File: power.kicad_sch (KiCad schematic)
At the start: 50 parts, among them J8 DeployLipo, J9 UCLipo, Q6 SI4143DY-T1-GE3, Q7 SI4143DY-T1-GE3, U10 NCP1117-3.3_SOT223, U11 XC8111, U12 XC8111, U13 XC8111, U14 LTC4412xS6, U15 MAX77827AEFD+T, U16 SC4215, U17 LTC4412xS6, U18 XC8111, U9 XC8111

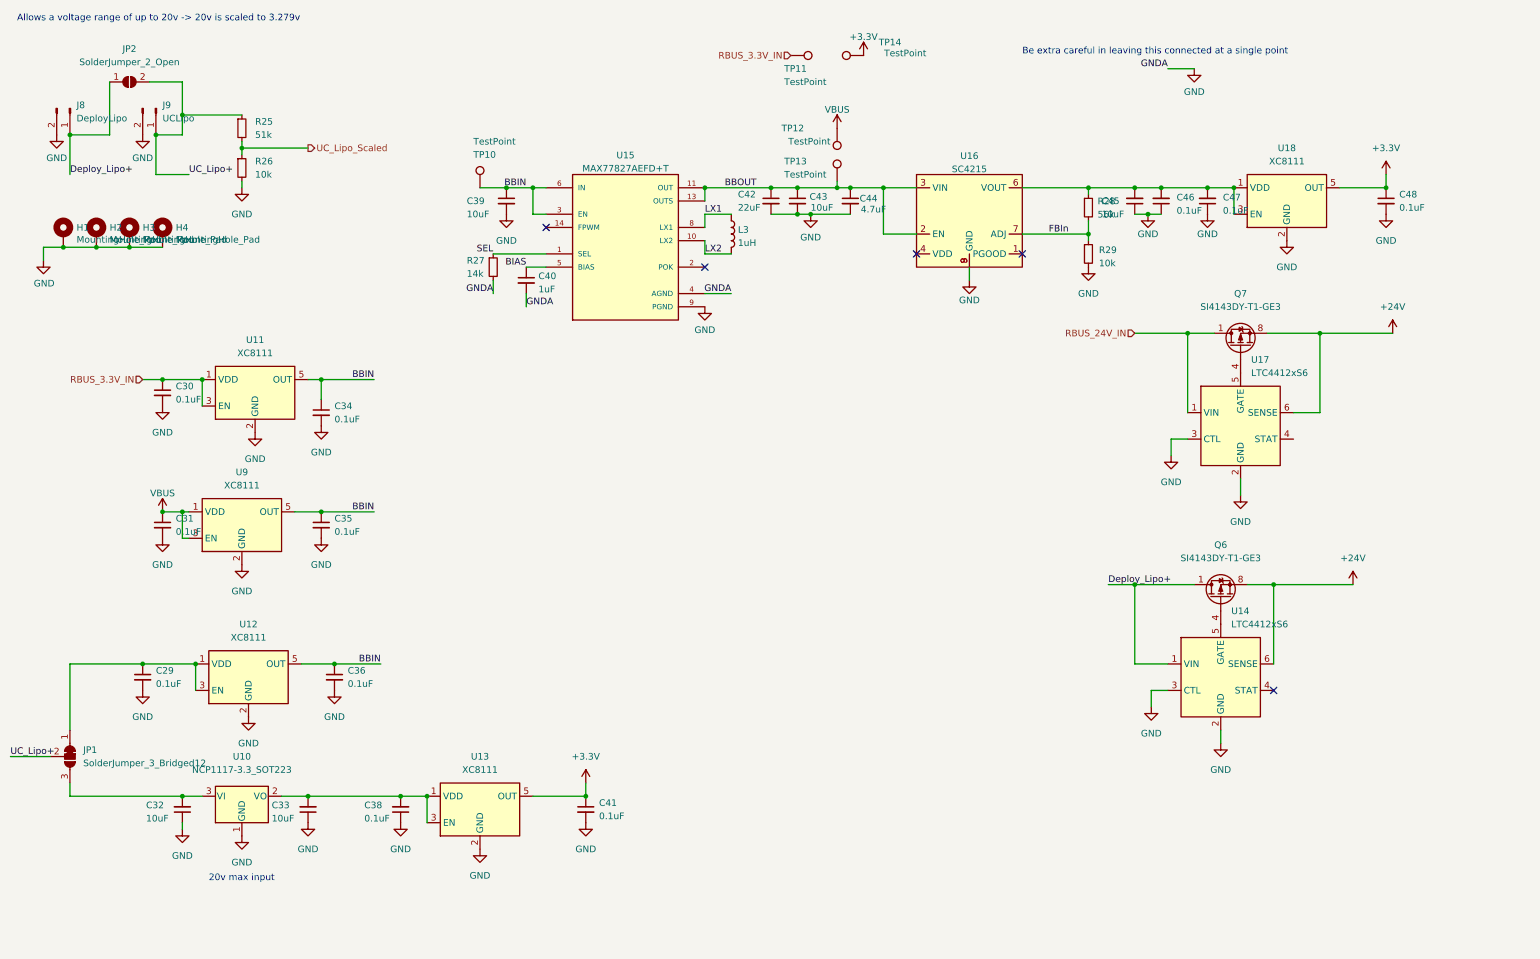
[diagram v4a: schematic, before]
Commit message: changed bb and power side
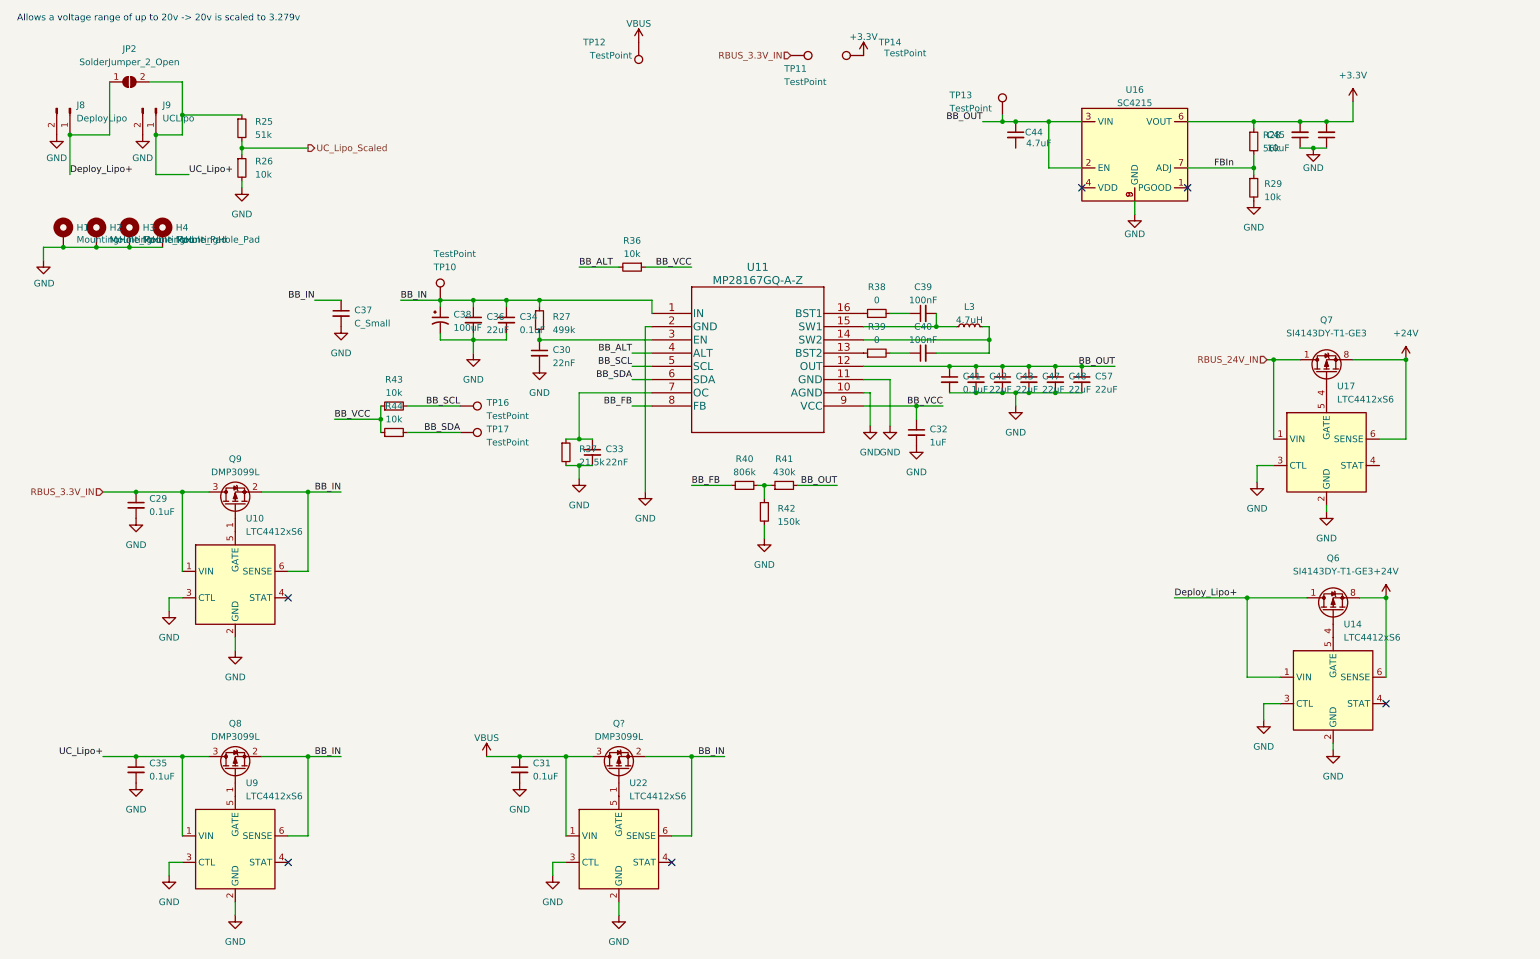
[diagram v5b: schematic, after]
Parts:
- removed C38: 0.1uF, Capacitor_SMD:C_0402_1005Metric, symbol Device:C_Small
- removed JP1: SolderJumper_3_Bridged12, Jumper:SolderJumper-3_P1.3mm_Bridged12_RoundedPad1.0x1.5mm, symbol Jumper:SolderJumper_3_Bridged12
- removed L3: 1uH, Inductor_SMD:L_0805_2012Metric, symbol Device:L
- removed U10: NCP1117-3.3_SOT223, Package_TO_SOT_SMD:SOT-223-3_TabPin2, symbol Regulator_Linear:NCP1117-3.3_SOT223
- removed U11, U12, U13, U18, U9: XC8111, Package_TO_SOT_SMD:SOT-23-5, symbol Analog_Switch:MAX40200AUK
- removed U15: MAX77827AEFD+T, iclr:CONV_MAX77827AEFD+T, symbol iclr:MAX77827AEFD+T
- added C37: C_Small, symbol Device:C_Small
- added C38: 100uF, symbol Device:C_Polarized_Small_US
- added C57: 22uF, symbol Device:C_Small
- added L3: 4.7uH, symbol Device:L_Small
- added Q8, Q9, Q?: DMP3099L, Package_TO_SOT_SMD:SOT-23, symbol Device:Q_PMOS_GSD
- added R36, R43, R44: 10k, symbol Device:R_Small
- added R37: 21.5k, symbol Device:R_Small
- added R38, R39: 0, symbol Device:R_Small
- added R40: 806k, symbol Device:R_Small
- added R41: 430k, symbol Device:R_Small
- added R42: 150k, symbol Device:R_Small
- added TP16, TP17: TestPoint, symbol Connector:TestPoint
- added U10, U22, U9: LTC4412xS6, Package_TO_SOT_SMD:TSOT-23-6, symbol Power_Management:LTC4412xS6
- added U11: MP28167GQ-A-Z, QFN-16_MP28167_MNP, symbol iclr:MP28167GQ-A-Z
- C30: value 0.1uF -> 22nF; footprint Capacitor_SMD:C_0402_1005Metric -> (none)
- C32: value 10uF -> 1uF; footprint Capacitor_SMD:C_0402_1005Metric -> (none)
- C33: value 10uF -> 22nF; footprint Capacitor_SMD:C_0402_1005Metric -> (none)
- C34, C41: footprint Capacitor_SMD:C_0402_1005Metric -> (none)
- C36, C47, C48: value 0.1uF -> 22uF; footprint Capacitor_SMD:C_0402_1005Metric -> (none)
- C39: value 10uF -> 100nF; footprint Capacitor_SMD:C_0603_1608Metric -> (none)
- C40: value 1uF -> 100nF; footprint Capacitor_SMD:C_0402_1005Metric -> (none)
- C42: footprint Capacitor_SMD:C_0603_1608Metric -> (none)
- C43: value 10uF -> 22uF; footprint Capacitor_SMD:C_0402_1005Metric -> (none)
- R27: value 14k -> 499k; footprint Resistor_SMD:R_0402_1005Metric -> (none)
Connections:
- net SEL is gone; now on net BB_IN: R27.1
- net +3V3: now also C45.2, C46.2, R28.1, U16.6 (VOUT); no longer C41.1, C48.1
- net GND: now also C32.2, C33.2, C47.2, C37.2, C38.2, C57.2, R37.2, R42.2, U10.2 (GND), U10.3 (CTL), U11.10 (AGND), U11.11 (GND), U11.2 (GND), U22.2 (GND), U22.3 (CTL), U9.2 (GND), U9.3 (CTL); no longer C32.1, C33.1, C39.2, C40.2, C44.2, C47.1, R27.2
- net RBUS_3.3V_IN: now also C29.1, Q9.3 (D), U10.1 (VIN); no longer C30.1
- net UC_Lipo+: now also C35.1, Q8.3 (D), U9.1 (VIN)
- net VBUS: now also Q?.3 (D), U22.1 (VIN)
- net BBIN renamed BB_IN
- net BB_IN: now also C37.1, C38.1, Q8.2 (S), Q9.2 (S), Q?.2 (S), U10.6 (SENSE), U11.1 (IN), U22.6 (SENSE), U9.6 (SENSE); no longer C35.1, C39.1
- net BBOUT renamed BB_OUT
- net BB_OUT: now also C41.1, C47.1, C48.1, C57.1, R41.2, U11.12 (OUT)
- net BIAS: no longer names the net of C40.1
- net BIAS: now also R39.2
- new net: C30.1, R27.2, U11.3 (EN)
- new net: Q8.1 (G), U9.5 (GATE)
- new net: C33.1, R37.1, U11.7 (OC)
- new net: Q9.1 (G), U10.5 (GATE)
- new net: Q?.1 (G), U22.5 (GATE)
- new net: R39.1, U11.13 (BST2)
- new net: R40.2, R41.1, R42.1
- new net: C40.2, L3.2, U11.14 (SW2)
- new net: C39.2, L3.1, U11.15 (SW1)
- new net: R38.1, U11.16 (BST1)
- new net: C39.1, R38.2
- new net BB_ALT: R36.2, U11.4 (ALT)
- new net BB_FB: R40.1, U11.8 (FB)
- new net BB_SCL: R43.2, TP16.1, U11.5 (SCL)
- new net BB_SDA: R44.2, TP17.1, U11.6 (SDA)
- new net BB_VCC: C32.1, R36.1, R43.1, R44.1, U11.9 (VCC)
- no-connect marks 5 -> 6
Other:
- note removed: "20v max input"
- note removed: "Be extra careful in leaving this connected at a single point"
- moved on the sheet: C44, C45, Q6, Q7, R28, R29, TP10, TP12, TP13, U14, U16, U17

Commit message: some updates?
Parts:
- removed L3: 4.7uH, symbol Device:L_Small
- added L3: MPL-AL6050-4R7, MPLAL60504R7, symbol iclr:MPL-AL6050-4R7
- C33: value 22nF -> 12nF
- R37: value 21.5k -> 37.4k
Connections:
- net at C40.2, U11.14 (SW2): now also L3.2
- net at C39.2, U11.15 (SW1): now also L3.1
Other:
- note added: "Current Limit set as 2.04A"
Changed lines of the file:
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@@
   (junction (at 111.76 160.02) (diameter 0) (color 0 0 0 0)
   )
+  (junction (at 201.93 80.01) (diameter 0) (color 0 0 0 0)
+  )
   (junction (at 278.13 129.54) (diameter 0) (color 0 0 0 0)
   )
@@
   )
   (junction (at 120.65 160.02) (diameter 0) (color 0 0 0 0)
-  )
-  (junction (at 201.93 80.01) (diameter 0) (color 0 0 0 0)
   )
   (junction (at 102.87 80.01) (diameter 0) (color 0 0 0 0)
@@
     (stroke (width 0) (type default))
   )
+  (wire (pts (xy 215.9 80.01) (xy 215.9 77.47))
+    (stroke (width 0) (type default))
+  )
   (wire (pts (xy 177.8 92.71) (xy 187.96 92.71))
     (stroke (width 0) (type default))
   )
-  (wire (pts (xy 201.93 77.47) (xy 200.66 77.47))
-    (stroke (width 0) (type default))
-  )
   (wire (pts (xy 20.32 62.23) (xy 20.32 64.77))
     (stroke (width 0) (type default))
@@
     (stroke (width 0) (type default))
   )
+  (wire (pts (xy 201.93 80.01) (xy 215.9 80.01))
+    (stroke (width 0) (type default))
+  )
   (wire (pts (xy 187.96 92.71) (xy 187.96 95.25))
     (stroke (width 0) (type default))
@@
   )
   (wire (pts (xy 144.78 107.95) (xy 152.4 107.95))
-    (stroke (width 0) (type default))
-  )
-  (wire (pts (xy 201.93 80.01) (xy 201.93 77.47))
     (stroke (width 0) (type default))
   )
@@
   (text "Allows a voltage range of up to 20v -> 20v is scaled to 3.279v"
     (at 15.24 19.05 0)
+    (effects (font (size 1.27 1.27)) (justify left bottom))
+  )
+  (text "Current Limit set as 2.04A" (at 95.25 106.68 0)
     (effects (font (size 1.27 1.27)) (justify left bottom))
   )
@@
       (effects (font (size 1.27 1.27)) (justify left))
     )
-    (property "Value" "21.5k" (at 123.19 103.505 0)
+    (property "Value" "37.4k" (at 123.19 103.505 0)
       (effects (font (size 1.27 1.27)) (justify left))
     )
@@
         (path "/e63e39d7-6ac0-4ffd-8aa3-1841a4541b55/150d7a0e-7d8c-4788-bc30-4a3682bf4d09"
           (reference "U10") (unit 1)
+        )
+      )
+    )
+  )
+  (symbol (lib_id "iclr:MPL-AL6050-4R7") (at 195.58 77.47 0) (unit 1)
+    (in_bom yes) (on_board yes) (dnp no) (fields_autoplaced)
+    (property "Reference" "L3" (at 205.74 72.39 0)
+      (effects (font (size 1.27 1.27)))
+    )
+    (property "Value" "MPL-AL6050-4R7" (at 205.74 74.93 0)
+      (effects (font (size 1.27 1.27)))
+    )
+    (property "Footprint" "MPLAL60504R7" (at 212.09 173.66 0)
+      (effects (font (size 1.27 1.27)) (justify left top) hide)
+    )
+    (property "Datasheet" "https://www.monolithicpower.com/en/documentview/productdocument/index/version/2/document_type/Datasheet/lang/en/sku/MPL-AL6050-4R7/document_id/5818/" (at 212.09 273.66 0)
+      (effects (font (size 1.27 1.27)) (justify left top) hide)
+    )
+    (property "Height" "5" (at 212.09 473.66 0)
+      (effects (font (size 1.27 1.27)) (justify left top) hide)
+    )
+    (property "Manufacturer_Name" "Monolithic Power Systems (MPS)" (at 212.09 573.66 0)
+      (effects (font (size 1.27 1.27)) (justify left top) hide)
+    )
+    (property "Manufacturer_Part_Number" "MPL-AL6050-4R7" (at 212.09 673.66 0)
+      (effects (font (size 1.27 1.27)) (justify left top) hide)
+    )
+    (property "Mouser Part Number" "946-MPL-AL6050-4R7" (at 212.09 773.66 0)
+      (effects (font (size 1.27 1.27)) (justify left top) hide)
+    )
+    (property "Mouser Price/Stock" "https://www.mouser.co.uk/ProductDetail/Monolithic-Power-Systems-MPS/MPL-AL6050-4R7?qs=sPbYRqrBIVlgVVgFJ%2Fjrsw%3D%3D" (at 212.09 873.66 0)
+      (effects (font (size 1.27 1.27)) (justify left top) hide)
+    )
+    (property "Arrow Part Number" "" (at 212.09 973.66 0)
+      (effects (font (size 1.27 1.27)) (justify left top) hide)
+    )
+    (property "Arrow Price/Stock" "" (at 212.09 1073.66 0)
+      (effects (font (size 1.27 1.27)) (justify left top) hide)
+    )
+    (pin "1")
+    (pin "2")
+    (instances
+      (project "PickleRick"
+        (path "/e63e39d7-6ac0-4ffd-8aa3-1841a4541b55/150d7a0e-7d8c-4788-bc30-4a3682bf4d09"
+          (reference "L3") (unit 1)
         )
       )
@@
       (effects (font (size 1.27 1.27)) (justify left))
     )
-    (property "Value" "22nF" (at 128.27 103.5113 0)
+    (property "Value" "12nF" (at 128.27 103.5113 0)
       (effects (font (size 1.27 1.27)) (justify left))
     )
@@
         )
       )
-    )
-  )
-  (symbol (lib_id "Device:L_Small") (at 198.12 77.47 90) (unit 1)
-    (in_bom yes) (on_board yes) (dnp no) (fields_autoplaced)
-    (property "Reference" "L3" (at 198.12 73.66 90)
-      (effects (font (size 1.27 1.27)))
-    )
-    (property "Value" "4.7uH" (at 198.12 76.2 90)
-      (effects (font (size 1.27 1.27)))
-    )
-    (property "Footprint" "" (at 198.12 77.47 0)
-      (effects (font (size 1.27 1.27)) hide)
-    )
-    (property "Datasheet" "~" (at 198.12 77.47 0)
-      (effects (font (size 1.27 1.27)) hide)
-    )
-    (pin "1")
-    (pin "2")
-    (instances
-      (project "PickleRick"
-        (path "/e63e39d7-6ac0-4ffd-8aa3-1841a4541b55/150d7a0e-7d8c-4788-bc30-4a3682bf4d09"
-          (reference "L3") (unit 1)
-        )
-      )

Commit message: did layout of buck kinda. 90% there
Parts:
- removed C37: C_Small, symbol Device:C_Small
- removed R38, R39: 0, symbol Device:R_Small
- removed TP12, TP14: TestPoint, TestPoint:TestPoint_Pad_D1.0mm, symbol Connector:TestPoint
- C30, C32, C33, C34, C39, C40, C41, C42, C43, C47, C48, C57, R27, R36, R37, R40, R41, R43, R44: footprint (none) -> Capacitor_SMD:C_0402_1005Metric
- C36: footprint (none) -> Capacitor_SMD:C_0805_2012Metric
- C38: footprint (none) -> Capacitor_SMD:CP_Elec_6.3x9.9
- L3: footprint MPLAL60504R7 -> iclr:MPLAL60504R7
- R25: value 51k -> 80k
- R42: value 150k -> 143k; footprint (none) -> Capacitor_SMD:C_0402_1005Metric
- TP10, TP11, TP13: footprint TestPoint:TestPoint_Pad_D1.0mm -> TestPoint:TestPoint_Pad_D2.0mm
- TP16, TP17: footprint (none) -> TestPoint:TestPoint_Pad_D1.0mm
- U11: footprint QFN-16_MP28167_MNP -> iclr:MP28167GQ-A-Z
- gave numbers to parts that had none: 1
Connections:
- net +3V3: now also TP11.1
- net RBUS_3.3V_IN: no longer TP11.1
- net at U11.13 (BST2): now also C40.1
- net at U11.16 (BST1): now also C39.1
- no-connect marks 6 -> 7
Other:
- note added: "Allows a voltage range of up to 30v -> 80k and 10k scaled to 3.333v"
- note added: "Vref = 1v R1 = (Vout - Vref)/Vref * R2 Aim for 4v due to max 600mv drop out on sc4215 R1 = 430k R2 = 143K"
- note removed: "Allows a voltage range of up to 20v -> 20v is scaled to 3.279v"
